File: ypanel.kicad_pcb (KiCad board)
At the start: 6 copper layers, 64 x 58 mm, 57 parts, among them IC2 TSL2561, J1 XF2M-1015-1A, J2 U.FL-R-SMT-1, J3 BATTERY CONNECTOR, J4 B2B-PH-SM4-TB_LF__SN_, U1 SWLP.12.B, U2 Value, U3 SW_SPDT, U4 SW_SPDT

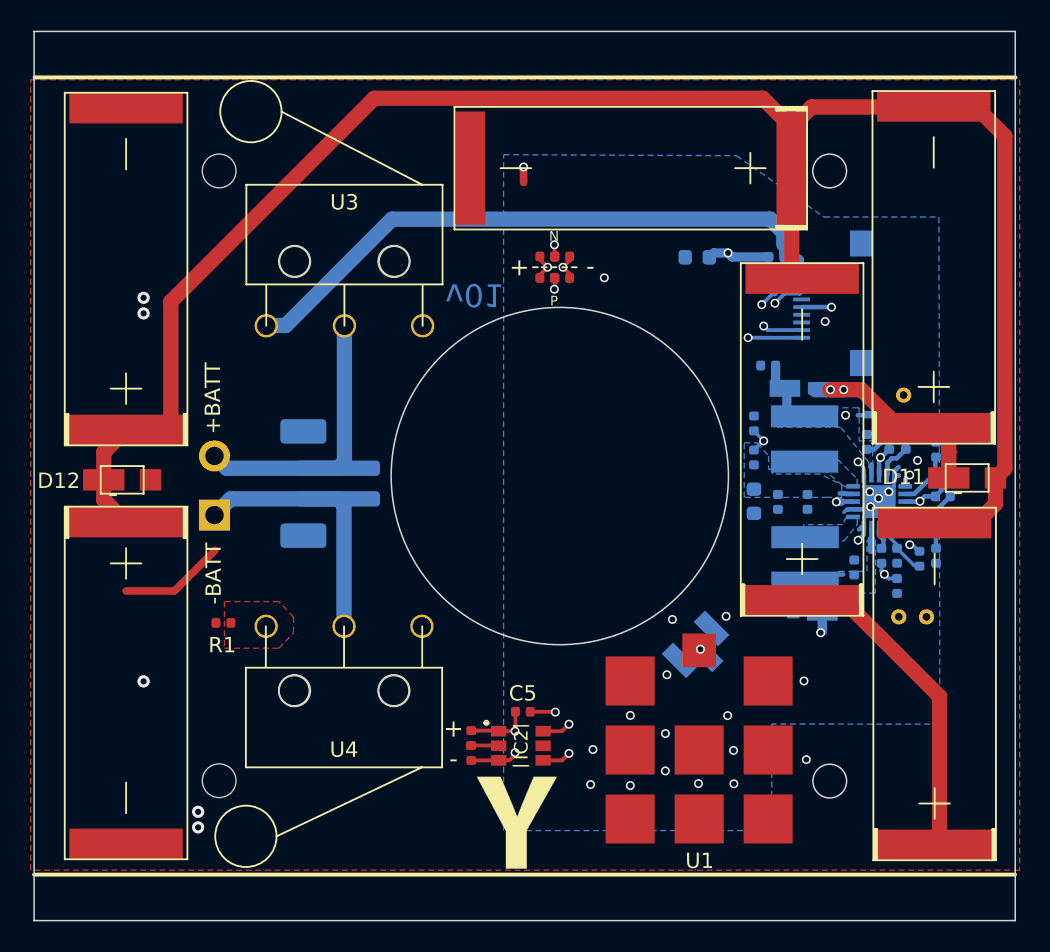
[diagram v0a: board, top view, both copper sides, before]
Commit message: repaired schematic so it matches PCB
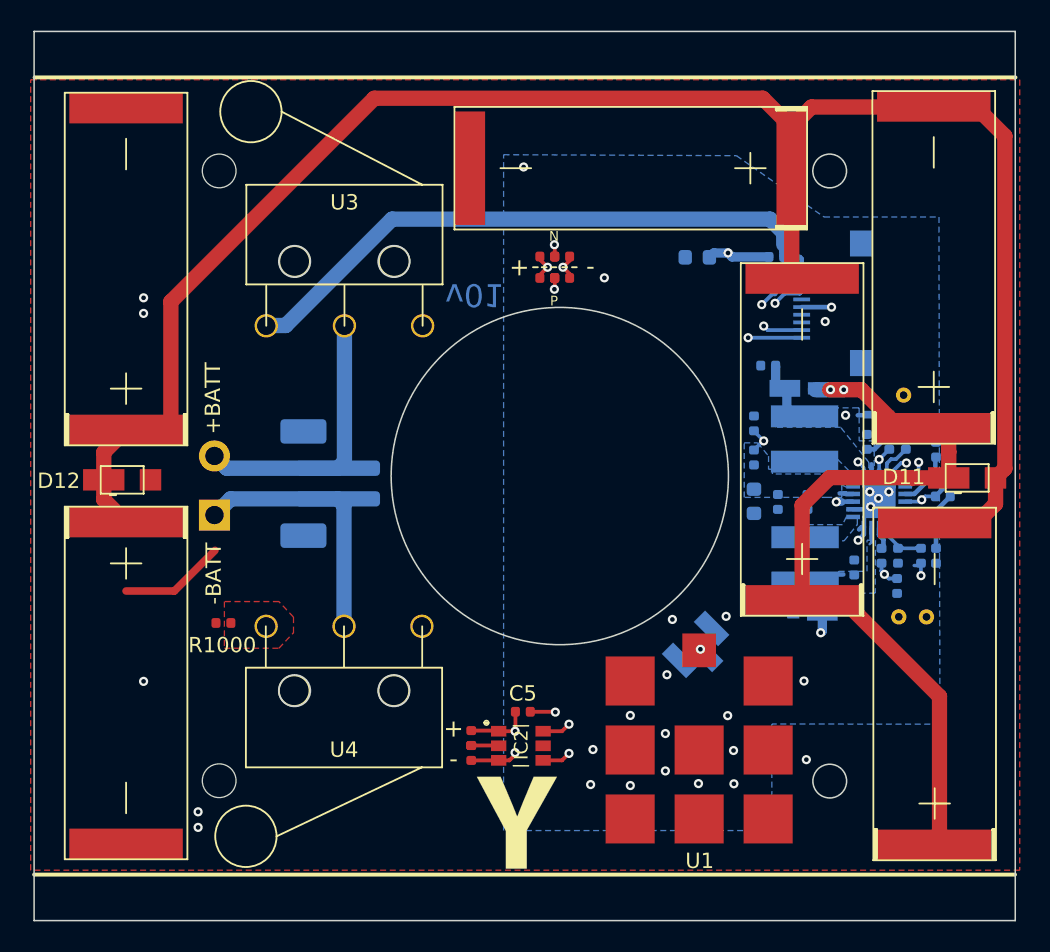
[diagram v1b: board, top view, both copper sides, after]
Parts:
- D1: value BZT52C4V7t -> SDM20U40-7
- D11, D12: value bypassdiode -> SBDiode
- R7: value 8.25M -> 4.75M
- R8: value 4.75M -> 8.25M
- SC1, SC2, SC3, SC4, SC5, SC6: value solarcell -> SolarCell_Small
- moved R8 1.56 mm to (170.8, 104.2), turned to 270 degrees
- moved R7 1.41 mm to (169.3, 104.2)
- renumbered R3 to R10, R1 to R1000, R4 to R16, R9 to R17, R10 to R18, R2 to R9
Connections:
- net /pre-3V3 renamed Net-(C7-Pad1)
- net Net-(D11-Pad1) renamed /VSOLAR_FULL
- IC2 pad 5: Net-(IC2-Pad5) -> (no net)
- J1 pad 5: BURN1 -> (no net)
- R7 pad 1: Net-(R7-Pad1) -> GND
- R7 pad 2: Net-(R2-Pad2) -> Net-(R7-Pad2)
- R8 pad 1: GND -> Net-(R7-Pad2)
- R8 pad 2: Net-(R7-Pad1) -> Net-(R2-Pad2)
- U2 pad 12: Net-(R7-Pad1) -> Net-(R7-Pad2)
- U3 pad 1: Net-(U3-Pad1) -> (no net)
- U4 pad 1: Net-(U4-Pad1) -> (no net)
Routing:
- net /VSOLAR_FULL: track 34.3 -> 50.8 mm
- net Net-(R7-Pad2): track 0.00 -> 3.80 mm
- net Net-(R7-Pad1): track 3.65 -> 0.00 mm
- net VOUT_EN: track 9.76 -> 12.1 mm
- net Net-(R2-Pad2): track 7.71 -> 9.97 mm
- net GND: track 22.7 -> 21.9 mm
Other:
- net class Default: trace_width 0.24892 -> 0.127; via_dia 0.5842 -> 0.6; via_drill 0.381 -> 0.3
- rule via_min_size: 0.45 -> 0.6

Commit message: Updated -Y
moved killswitches & flat-flex connector to new locations
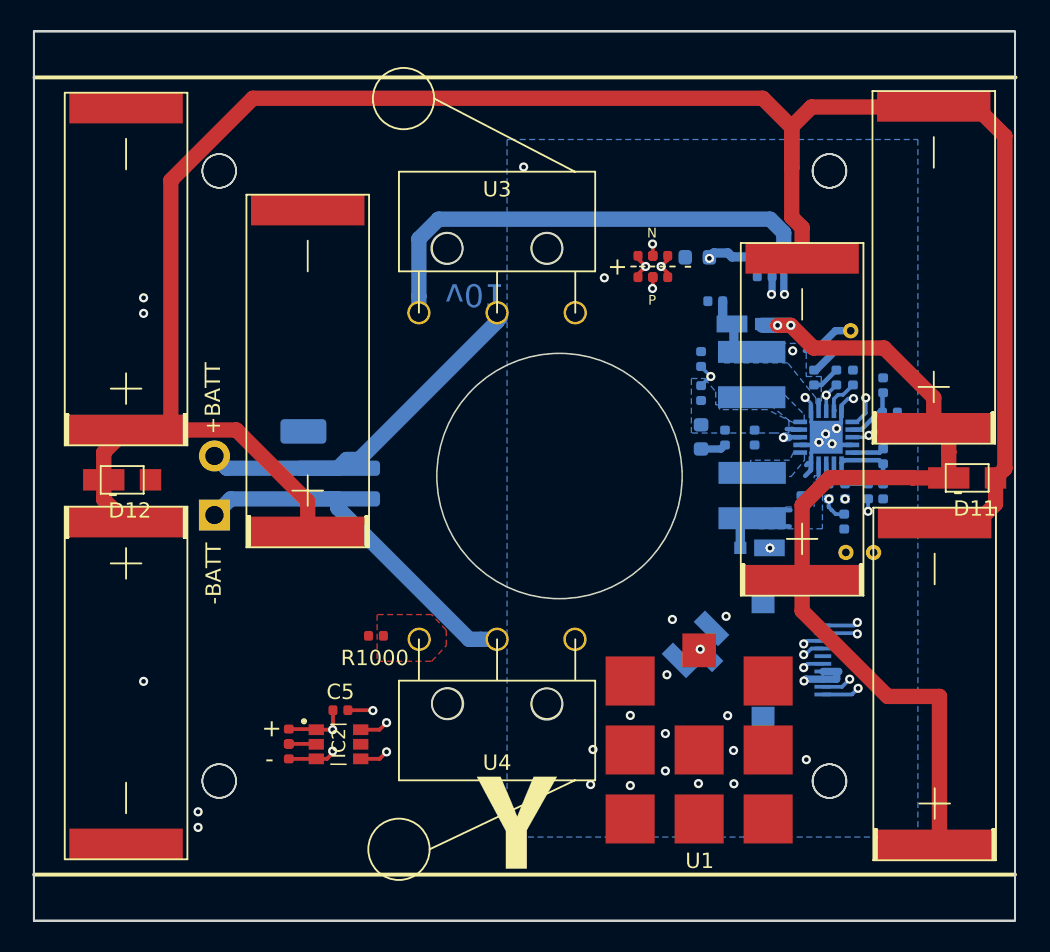
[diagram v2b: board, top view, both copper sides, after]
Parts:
- D11, D12: footprint solarpcb:SB-Diode -> SolarCellParts:SB Diode
- moved SC4 39.5 mm to (130.8, 102.7), turned to 90 degrees
- moved J1 23.3 mm to (164.4, 111.0), turned to 90 degrees
- moved C5 11.9 mm to (133.0, 114.3)
- moved IC2 11.9 mm to (132.9, 116.5)
- moved R17 11.9 mm to (129.6, 116.0)
- moved R18 11.9 mm to (129.6, 117.0)
- moved U4 10.0 mm to (143.2, 109.7)
- moved U3 9.99 mm to (143.2, 88.3)
- moved R1000 9.99 mm to (135.3, 109.4)
- moved R10 6.40 mm to (153.8, 86.0)
- moved R16 6.40 mm to (152.9, 84.6)
- moved R19 6.40 mm to (153.8, 84.6)
- moved R9 6.40 mm to (152.9, 86.0)
- moved C4 5.44 mm to (166.4, 92.6)
- moved C7 5.44 mm to (163.0, 100.8)
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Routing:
- net BATT_N: track 2.50 -> 34.9 mm, vias 0 -> 2
- net COIL_N: track 19.5 -> 50.9 mm
- net COIL_P: track 18.2 -> 49.1 mm
- net BATT_P: track 41.9 -> 62.4 mm, vias 0 -> 2
- net /coil: track 15873.0 -> 15890.0 mm
- net Net-(D11-Pad2): track 123.3 -> 136.9 mm
- net SCL1: track 42.9 -> 33.1 mm
- net SDA1: track 42.0 -> 32.8 mm
- net /VSOLAR_FULL: track 50.8 -> 59.8 mm
- net +3V3: track 60.8 -> 53.5 mm
- net /VBAT: track 25.3 -> 18.9 mm
- net Net-(J3-Pad1): track 17.0 -> 23.0 mm
- net Net-(J3-Pad2): track 17.8 -> 23.1 mm
- net VSOLAR: track 10.7 -> 9.21 mm
- net VOUT_EN: track 12.1 -> 11.4 mm
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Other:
- outline, holes or cut-outs redrawn
